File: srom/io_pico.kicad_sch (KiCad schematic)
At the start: 4 parts, among them J201 Conn_01x03_Female, U201 Pico-2 IO, U202 74LS245

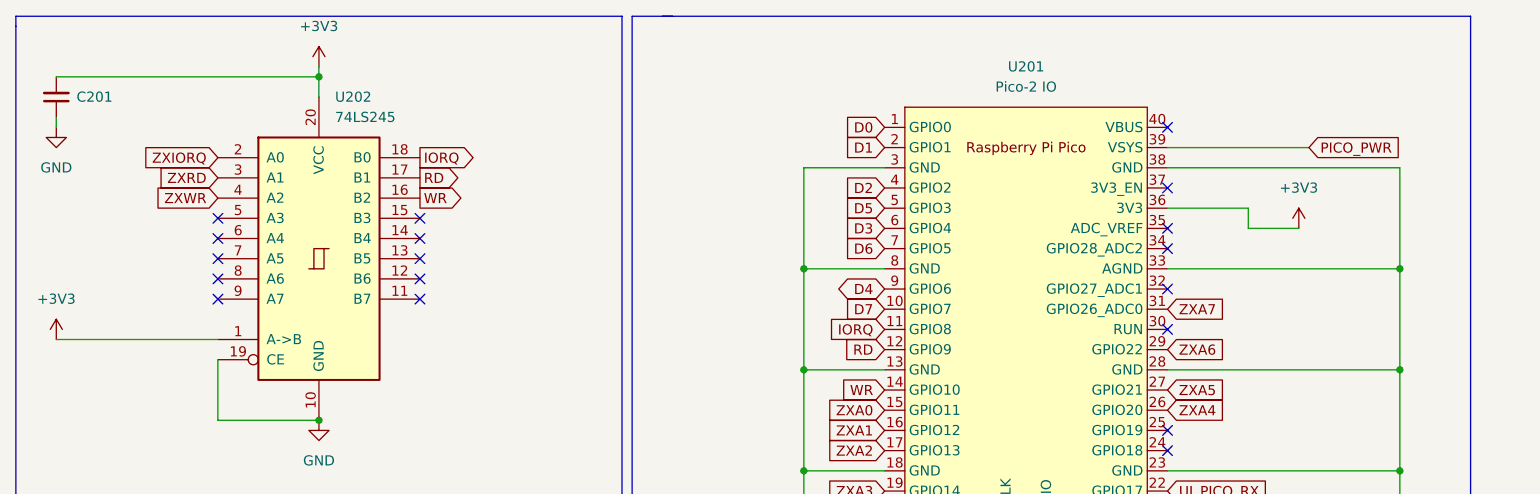
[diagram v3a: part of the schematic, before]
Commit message: break out the 3V3 supplies into separate ones
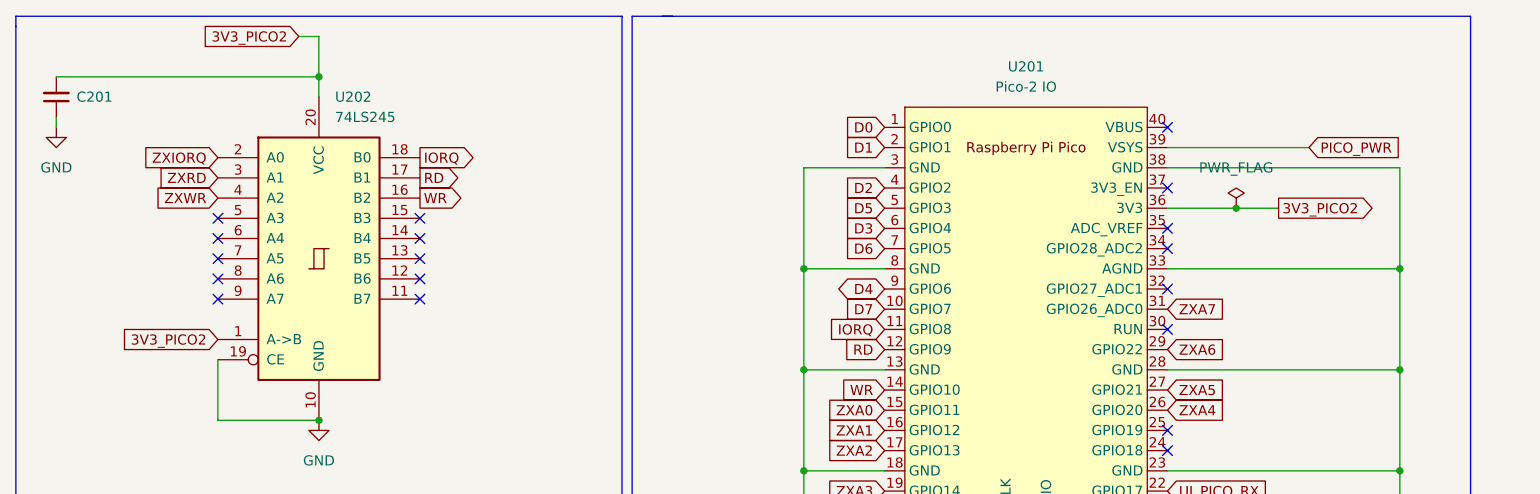
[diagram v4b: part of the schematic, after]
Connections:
- net +3V3 renamed 3V3_PICO2
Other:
- title: ZX Spectrum IF1 ROM -> Pico Interface One
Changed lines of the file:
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@@
   (paper "A4")
   (title_block
-    (title "ZX Spectrum IF1 ROM")
-    (date "2023-02-07")
-    (rev "1.0")
+    (title "Pico Interface One")
+    (date "2023-03-01")
+    (rev "v1.1 to v1.2 WIP")
   )
   (junction (at 191.77 125.73) (diameter 0) (color 0 0 0 0)
   )
   (junction (at 116.84 80.01) (diameter 0) (color 0 0 0 0)
+  )
+  (junction (at 171.196 59.69) (diameter 0) (color 0 0 0 0)
   )
   (junction (at 116.84 92.71) (diameter 0) (color 0 0 0 0)
@@
   (no_connect (at 162.56 87.63))
   (no_connect (at 162.56 74.93))
-  (wire (pts (xy 22.86 76.2) (xy 43.18 76.2))
+  (wire (pts (xy 53.34 38.1) (xy 55.88 38.1))
     (stroke (width 0) (type default) (color 0 0 0 0))
   )
@@
     (stroke (width 0) (type default) (color 0 0 0 0))
   )
+  (wire (pts (xy 55.88 38.1) (xy 55.88 43.18))
+    (stroke (width 0) (type default) (color 0 0 0 0))
+  )
   (wire (pts (xy 116.84 54.61) (xy 116.84 67.31))
     (stroke (width 0) (type default) (color 0 0 0 0))
@@
     (stroke (width 0) (type default) (color 0 0 0 0))
   )
-  (wire (pts (xy 55.88 41.91) (xy 55.88 43.18))
-    (stroke (width 0) (type default) (color 0 0 0 0))
-  )
   (wire (pts (xy 116.84 92.71) (xy 116.84 125.73))
     (stroke (width 0) (type default) (color 0 0 0 0))
   )
-  (wire (pts (xy 172.72 59.69) (xy 172.72 62.23))
-    (stroke (width 0) (type default) (color 0 0 0 0))
-  )
   (wire (pts (xy 43.18 78.74) (xy 43.18 86.36))
     (stroke (width 0) (type default) (color 0 0 0 0))
@@
     (stroke (width 0) (type default) (color 0 0 0 0))
   )
-  (wire (pts (xy 162.56 59.69) (xy 172.72 59.69))
-    (stroke (width 0) (type default) (color 0 0 0 0))
-  )
   (wire (pts (xy 116.84 67.31) (xy 116.84 80.01))
     (stroke (width 0) (type default) (color 0 0 0 0))
@@
     (stroke (width 0) (type default) (color 0 0 0 0))
   )
-  (wire (pts (xy 172.72 62.23) (xy 179.07 62.23))
+  (wire (pts (xy 162.56 59.69) (xy 171.196 59.69))
     (stroke (width 0) (type default) (color 0 0 0 0))
   )
@@
   )
   (polyline (pts (xy 93.98 35.56) (xy 93.98 107.95))
+    (stroke (width 0) (type default) (color 0 0 0 0))
+  )
+  (wire (pts (xy 171.196 59.69) (xy 176.53 59.69))
     (stroke (width 0) (type default) (color 0 0 0 0))
   )
@@
     )
   )
+  (global_label "3V3_PICO2" (shape output) (at 176.53 59.69 0) (fields_autoplaced)
+    (effects (font (size 1.27 1.27)) (justify left))
+    (property "Intersheet References" "${INTERSHEET_REFS}" (id 0) (at 189.1031 59.6106 0)
+      (effects (font (size 1.27 1.27)) (justify left) hide)
+    )
+  )
   (global_label "PICO_PWR" (shape input) (at 180.34 52.07 0) (fields_autoplaced)
     (effects (font (size 1.27 1.27)) (justify left))
@@
     )
   )
+  (global_label "3V3_PICO2" (shape input) (at 43.18 76.2 180) (fields_autoplaced)
+    (effects (font (size 1.27 1.27)) (justify right))
+    (property "Intersheet References" "${INTERSHEET_REFS}" (id 0) (at 30.6069 76.2794 0)
+      (effects (font (size 1.27 1.27)) (justify right) hide)
+    )
+  )
   (global_label "ZXA4" (shape input) (at 162.56 85.09 0) (fields_autoplaced)
     (effects (font (size 1.27 1.27)) (justify left))
@@
     )
   )
+  (global_label "3V3_PICO2" (shape input) (at 53.34 38.1 180) (fields_autoplaced)
+    (effects (font (size 1.27 1.27)) (justify right))
+    (property "Intersheet References" "${INTERSHEET_REFS}" (id 0) (at 40.7669 38.0206 0)
+      (effects (font (size 1.27 1.27)) (justify right) hide)
+    )
+  )
   (global_label "D3" (shape input) (at 127 62.23 180) (fields_autoplaced)
     (effects (font (size 1.27 1.27)) (justify right))
@@
     )
   )
-  (symbol (lib_id "power:+3V3") (at 22.86 76.2 0) (unit 1)
+  (symbol (lib_id "power:PWR_FLAG") (at 171.196 59.69 0) (unit 1)
     (in_bom yes) (on_board yes) (fields_autoplaced)
-    (property "Reference" "#PWR0205" (id 0) (at 22.86 80.01 0)
-      (effects (font (size 1.27 1.27)) hide)
-    )
-    (property "Value" "+3V3" (id 1) (at 22.86 71.12 0))
-    (property "Footprint" "" (id 2) (at 22.86 76.2 0)
-      (effects (font (size 1.27 1.27)) hide)
-    )
-    (property "Datasheet" "" (id 3) (at 22.86 76.2 0)
+    (property "Reference" "#FLG0103" (id 0) (at 171.196 57.785 0)
+      (effects (font (size 1.27 1.27)) hide)
+    )
+    (property "Value" "PWR_FLAG" (id 1) (at 171.196 54.61 0))
+    (property "Footprint" "" (id 2) (at 171.196 59.69 0)
+      (effects (font (size 1.27 1.27)) hide)
+    )
+    (property "Datasheet" "~" (id 3) (at 171.196 59.69 0)
       (effects (font (size 1.27 1.27)) hide)
     )
@@
       (effects (font (size 1.27 1.27)) hide)
     )
-    (pin "1")
-  )
-  (symbol (lib_id "power:+3V3") (at 179.07 62.23 0) (unit 1)
-    (in_bom yes) (on_board yes)
-    (property "Reference" "#PWR0202" (id 0) (at 179.07 66.04 0)
-      (effects (font (size 1.27 1.27)) hide)
-    )
-    (property "Value" "+3V3" (id 1) (at 179.07 57.15 0))
-    (property "Footprint" "" (id 2) (at 179.07 62.23 0)
-      (effects (font (size 1.27 1.27)) hide)
-    )
-    (property "Datasheet" "" (id 3) (at 179.07 62.23 0)
-      (effects (font (size 1.27 1.27)) hide)
-    )
-    (pin "1")
-  )
-  (symbol (lib_id "power:+3V3") (at 55.88 41.91 0) (unit 1)
-    (in_bom yes) (on_board yes) (fields_autoplaced)
-    (property "Reference" "#PWR0206" (id 0) (at 55.88 45.72 0)
-      (effects (font (size 1.27 1.27)) hide)
-    )
-    (property "Value" "+3V3" (id 1) (at 55.88 36.83 0))
-    (property "Footprint" "" (id 2) (at 55.88 41.91 0)
-      (effects (font (size 1.27 1.27)) hide)
-    )
-    (property "Datasheet" "" (id 3) (at 55.88 41.91 0)
-      (effects (font (size 1.27 1.27)) hide)
-    )

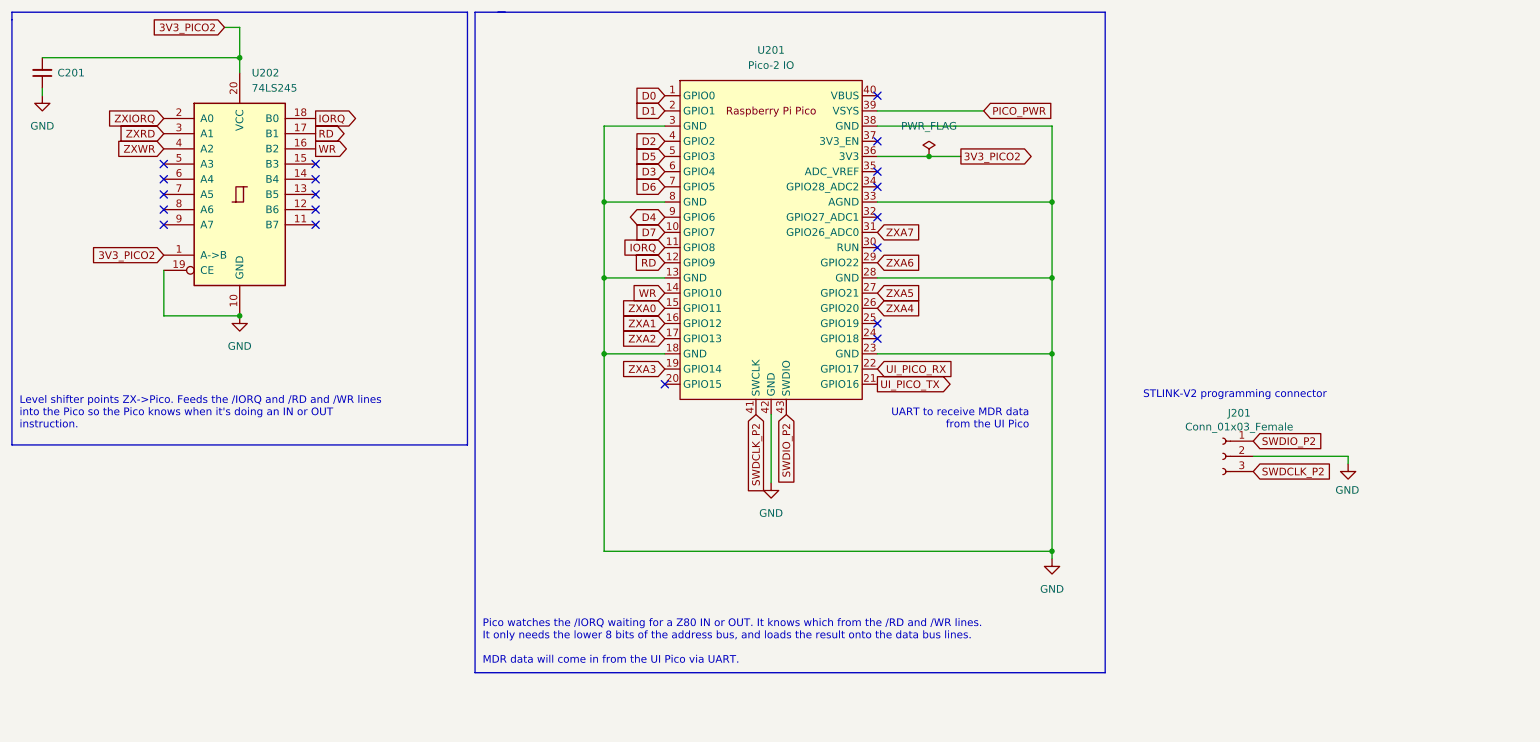
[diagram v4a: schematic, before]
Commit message: update schematic to match my modified prototype hardware
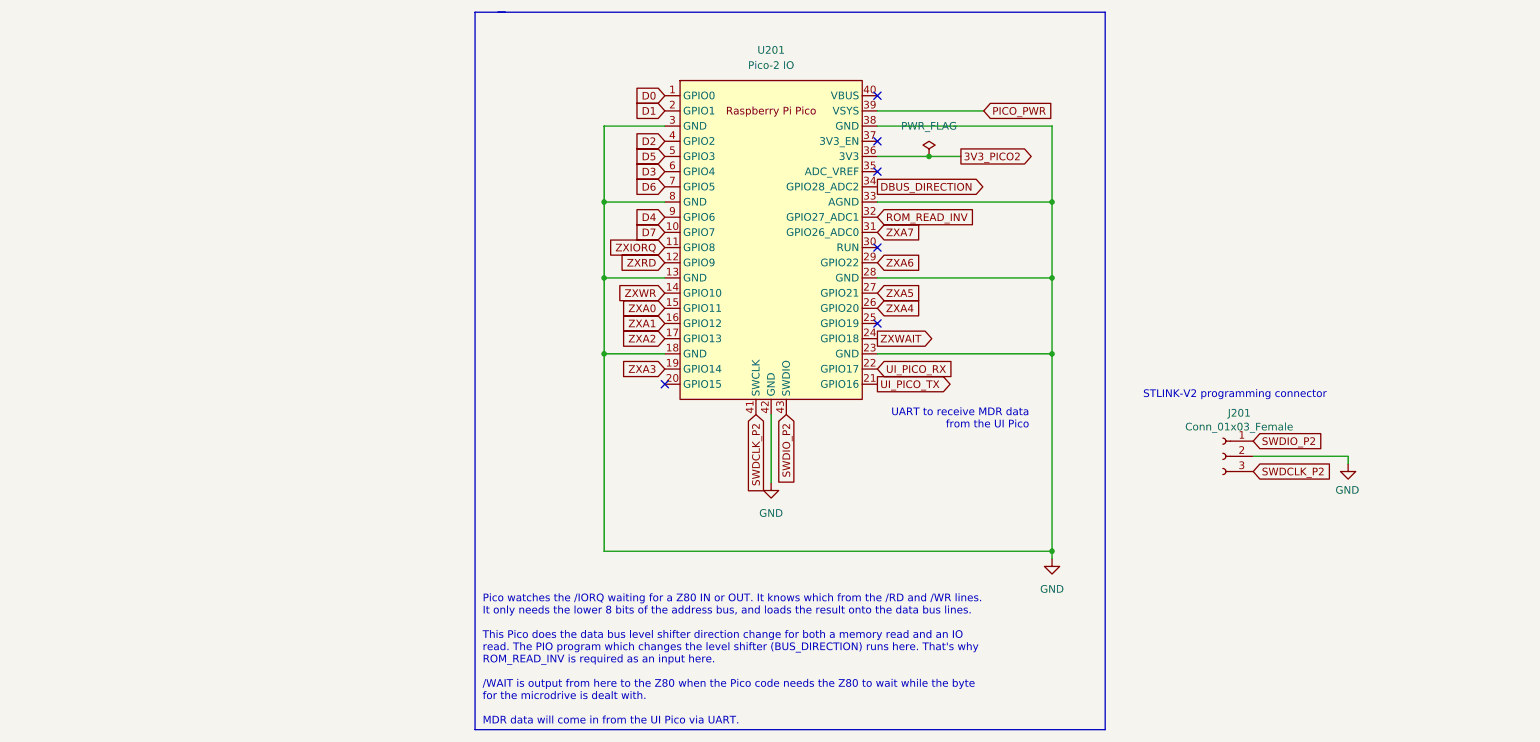
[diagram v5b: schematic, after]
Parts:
- removed C201: C_Small, Capacitor_SMD:C_1206_3216Metric, symbol Device:C_Small
- removed U202: 74LS245, Package_SO:SO-20_5.3x12.6mm_P1.27mm, symbol 74xx:74LS245
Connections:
- net IORQ is gone; now on net ZXIORQ: U201.11 (GPIO8)
- net RD is gone; now on net ZXRD: U201.12 (GPIO9)
- net WR is gone; now on net ZXWR: U201.14 (GPIO10)
- net ZXWAIT: now reaches U201.24 (GPIO18)
- net ROM_READ_INV: now reaches U201.32 (GPIO27_ADC1)
- net DBUS_DIRECTION: now reaches U201.34 (GPIO28_ADC2)
- no-connect marks 19 -> 6
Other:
- note added: "Pico watches the /IORQ waiting for a Z80 IN or OUT. It knows which from the /RD and /WR lines. It only needs the lower 8 bits of the address bus, and loads the result onto the data bus lines. This Pico does the data bus level shifter direction change for both a memory read and an IO read. The PIO program which changes the level shifter (BUS_DIRECTION) runs here. That's why ROM_READ_INV is require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"
- note removed: "Level shifter points ZX->Pico. Feeds the /IORQ and /RD and /WR lines into the Pico so the Pico knows when it's doing an IN or OUT instruction."
- note removed: "Pico watches the /IORQ waiting for a Z80 IN or OUT. It knows which from the /RD and /WR lines. It only needs the lower 8 bits of the address bus, and loads the result onto the data bus lines. MDR data will come in from the UI Pico via UART."

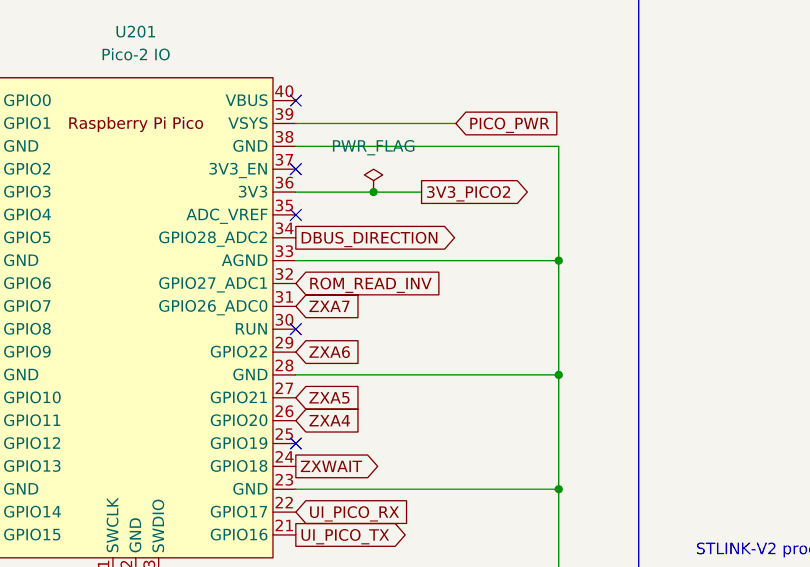
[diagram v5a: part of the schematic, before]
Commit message: start v1.3 of board, level shifter required
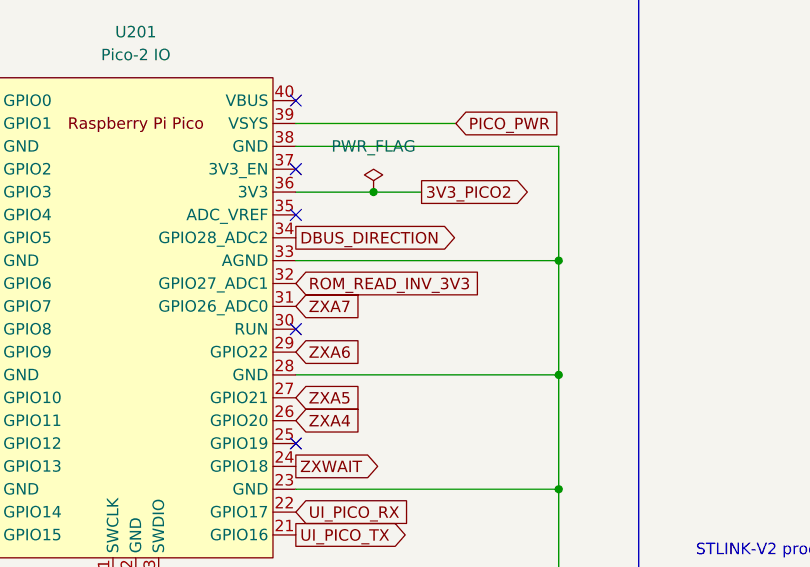
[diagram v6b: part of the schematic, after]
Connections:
- net ROM_READ_INV renamed ROM_READ_INV_3V3
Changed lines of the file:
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@@
   (title_block
     (title "Pico Interface One")
-    (date "2023-03-01")
-    (rev "v1.1 to v1.2 WIP")
+    (date "2023-04-13")
+    (rev "v1.2 to v1.3 WIP")
   )
   (junction (at 191.77 125.73) (diameter 0) (color 0 0 0 0)
@@
     )
   )
-  (global_label "ROM_READ_INV" (shape input) (at 162.56 69.85 0) (fields_autoplaced)
-    (effects (font (size 1.27 1.27)) (justify left))
-    (property "Intersheet References" "${INTERSHEET_REFS}" (id 0) (at 178.7617 69.7706 0)
-      (effects (font (size 1.27 1.27)) (justify left) hide)
-    )
+  (global_label "ROM_READ_INV_3V3" (shape input) (at 162.56 69.85 0) (fields_autoplaced)
+    (effects (font (size 1.27 1.27)) (justify left))
+    (property "Intersheet References" "${INTERSHEET_REFS}" (id 0) (at 183.2369 69.7706 0)
+      (effects (font (size 1.27 1.27)) (justify left) hide)
+    )
